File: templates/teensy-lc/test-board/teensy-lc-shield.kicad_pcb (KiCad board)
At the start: 2 copper layers, 1 part, among them J1 TEENSY LC

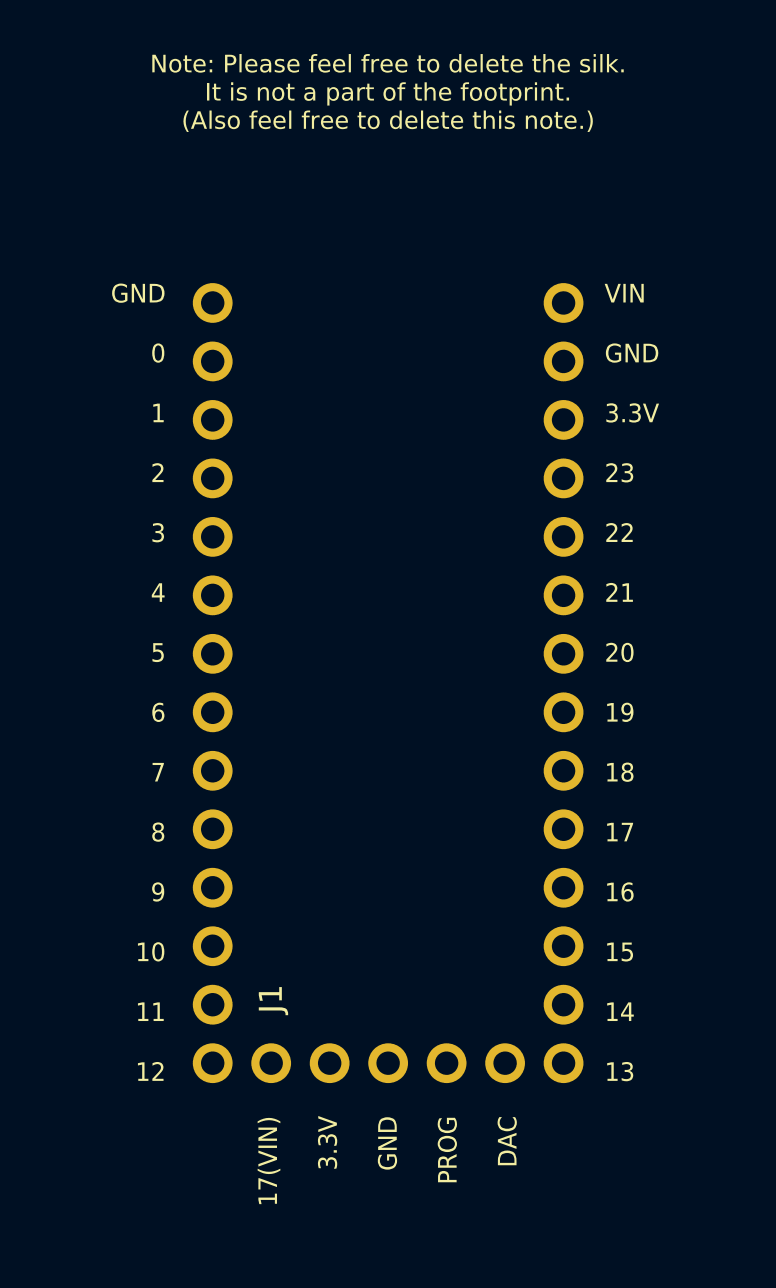
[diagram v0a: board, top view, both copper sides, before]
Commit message: Added Teensy LC bare template and test board.
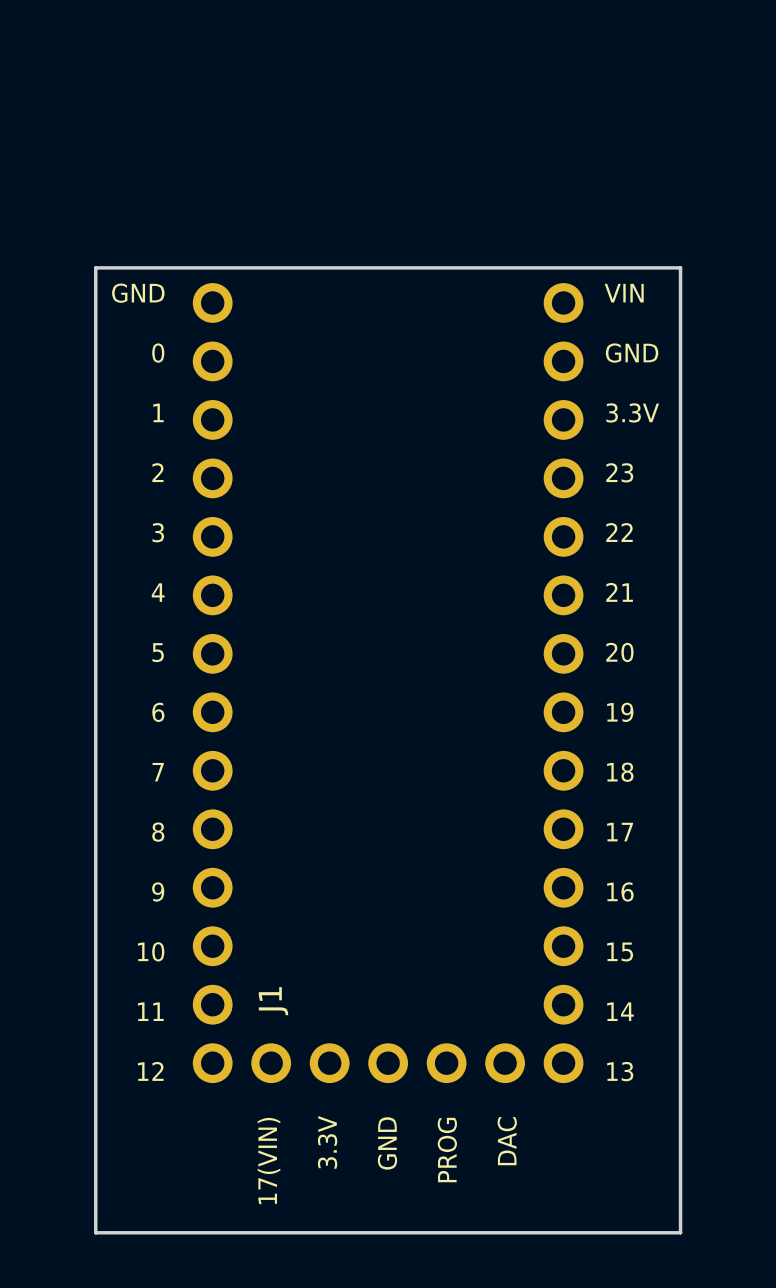
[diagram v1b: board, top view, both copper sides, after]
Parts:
- added REF**: Symbol_OSHW-Logo_SilkScreen, Wickerlib:Symbol_OSHW-Logo_SilkScreen, B.Cu at (102.9, 85.1)
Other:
- board outline added: 25.4 x 41.9 mm
- board text added: "TEMPLATE TEST BOARD"
- board text removed: "Note: Please feel free to delete the silk. It is not a part of the footprint. (Also feel free to delete this note.)"
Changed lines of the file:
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@@
 (kicad_pcb (version 4) (host pcbnew 4.0.1-3.201512221402+6198~38~ubuntu14.04.1-stable)
   (general
-    (links 3)
+    (links 0)
     (no_connects 3)
     (area 90.094999 71.043799 178.510001 123.265001)
     (thickness 1.6)
-    (drawings 21)
+    (drawings 25)
     (tracks 0)
     (zones 0)
-    (modules 1)
+    (modules 2)
     (nets 3)
   )
@@
     (pad 15 thru_hole circle (at 5.08 17.78) (size 1.7272 1.7272) (drill 1.016) (layers *.Cu *.Mask F.SilkS))
   )
-  (gr_text "Note: Please feel free to delete the silk.\nIt is not a part of the footprint.\n(Also feel free to delete this note.)" (at 102.87 63.5) (layer F.SilkS)
-    (effects (font (size 0.762 0.762) (thickness 0.1524)))
+  (module Wickerlib:Symbol_OSHW-Logo_SilkScreen (layer B.Cu)
+    (at 102.87 85.09 180)
+    (descr "Symbol, OSHW-Logo, Silk Screen,")
+    (tags "Symbol, OSHW-Logo, Silk Screen,")
+    (fp_text reference REF** (at 0.09906 4.38912 180) (layer B.SilkS) hide
+      (effects (font (size 1 1) (thickness 0.15)) (justify mirror))
+    )
+    (fp_text value Symbol_OSHW-Logo_SilkScreen (at 0.30988 -6.56082 180) (layer B.Fab)
+      (effects (font (size 1 1) (thickness 0.15)) (justify mirror))
+    )
+    (fp_line (start 1.66878 -2.68986) (end 2.02946 -4.16052) (layer B.SilkS) (width 0.15))
+    (fp_line (start 2.02946 -4.16052) (end 2.30886 -3.0988) (layer B.SilkS) (width 0.15))
+    (fp_line (start 2.30886 -3.0988) (end 2.61874 -4.17068) (layer B.SilkS) (width 0.15))
+    (fp_line (start 2.61874 -4.17068) (end 2.9591 -2.72034) (layer B.SilkS) (width 0.15))
+    (fp_line (start 0.24892 -3.38074) (end 1.03886 -3.37058) (layer B.SilkS) (width 0.15))
+    (fp_line (start 1.03886 -3.37058) (end 1.04902 -3.38074) (layer B.SilkS) (width 0.15))
+    (fp_line (start 1.04902 -3.38074) (end 1.04902 -3.37058) (layer B.SilkS) (width 0.15))
+    (fp_line (start 1.08966 -2.65938) (end 1.08966 -4.20116) (layer B.SilkS) (width 0.15))
+    (fp_line (start 0.20066 -2.64922) (end 0.20066 -4.21894) (layer B.SilkS) (width 0.15))
+    (fp_line (start 0.20066 -4.21894) (end 0.21082 -4.20878) (layer B.SilkS) (width 0.15))
+    (fp_line (start -0.35052 -2.75082) (end -0.70104 -2.66954) (layer B.SilkS) (width 0.15))
+    (fp_line (start -0.70104 -2.66954) (end -1.02108 -2.65938) (layer B.SilkS) (width 0.15))
+    (fp_line (start -1.02108 -2.65938) (end -1.25984 -2.86004) (layer B.SilkS) (width 0.15))
+    (fp_line (start -1.25984 -2.86004) (end -1.29032 -3.12928) (layer B.SilkS) (width 0.15))
+    (fp_line (start -1.29032 -3.12928) (end -1.04902 -3.37058) (layer B.SilkS) (width 0.15))
+    (fp_line (start -1.04902 -3.37058) (end -0.6604 -3.50012) (layer B.SilkS) (width 0.15))
+    (fp_line (start -0.6604 -3.50012) (end -0.48006 -3.66014) (layer B.SilkS) (width 0.15))
+    (fp_line (start -0.48006 -3.66014) (end -0.43942 -3.95986) (layer B.SilkS) (width 0.15))
+    (fp_line (start -0.43942 -3.95986) (end -0.67056 -4.18084) (layer B.SilkS) (width 0.15))
+    (fp_line (start -0.67056 -4.18084) (end -0.9906 -4.20878) (layer B.SilkS) (width 0.15))
+    (fp_line (start -0.9906 -4.20878) (end -1.34112 -4.09956) (layer B.SilkS) (width 0.15))
+    (fp_line (start -2.37998 -2.64922) (end -2.6289 -2.66954) (layer B.SilkS) (width 0.15))
+    (fp_line (start -2.6289 -2.66954) (end -2.8702 -2.91084) (layer B.SilkS) (width 0.15))
+    (fp_line (start -2.8702 -2.91084) (end -2.9591 -3.40106) (layer B.SilkS) (width 0.15))
+    (fp_line (start -2.9591 -3.40106) (end -2.93116 -3.74904) (layer B.SilkS) (width 0.15))
+    (fp_line (start -2.93116 -3.74904) (end -2.7305 -4.06908) (layer B.SilkS) (width 0.15))
+    (fp_line (start -2.7305 -4.06908) (end -2.47904 -4.191) (layer B.SilkS) (width 0.15))
+    (fp_line (start -2.47904 -4.191) (end -2.16916 -4.11988) (layer B.SilkS) (width 0.15))
+    (fp_line (start -2.16916 -4.11988) (end -1.95072 -3.93954) (layer B.SilkS) (width 0.15))
+    (fp_line (start -1.95072 -3.93954) (end -1.8796 -3.4798) (layer B.SilkS) (width 0.15))
+    (fp_line (start -1.8796 -3.4798) (end -1.9304 -3.07086) (layer B.SilkS) (width 0.15))
+    (fp_line (start -1.9304 -3.07086) (end -2.03962 -2.78892) (layer B.SilkS) (width 0.15))
+    (fp_line (start -2.03962 -2.78892) (end -2.4003 -2.65938) (layer B.SilkS) (width 0.15))
+    (fp_line (start -1.78054 -0.92964) (end -2.03962 -1.49098) (layer B.SilkS) (width 0.15))
+    (fp_line (start -2.03962 -1.49098) (end -1.50114 -2.00914) (layer B.SilkS) (width 0.15))
+    (fp_line (start -1.50114 -2.00914) (end -0.98044 -1.7399) (layer B.SilkS) (width 0.15))
+    (fp_line (start -0.98044 -1.7399) (end -0.70104 -1.89992) (layer B.SilkS) (width 0.15))
+    (fp_line (start 0.73914 -1.8796) (end 1.06934 -1.6891) (layer B.SilkS) (width 0.15))
+    (fp_line (start 1.06934 -1.6891) (end 1.50876 -2.0193) (layer B.SilkS) (width 0.15))
+    (fp_line (start 1.50876 -2.0193) (end 1.9812 -1.52908) (layer B.SilkS) (width 0.15))
+    (fp_line (start 1.9812 -1.52908) (end 1.69926 -1.04902) (layer B.SilkS) (width 0.15))
+    (fp_line (start 1.69926 -1.04902) (end 1.88976 -0.57912) (layer B.SilkS) (width 0.15))
+    (fp_line (start 1.88976 -0.57912) (end 2.49936 -0.39116) (layer B.SilkS) (width 0.15))
+    (fp_line (start 2.49936 -0.39116) (end 2.49936 0.28956) (layer B.SilkS) (width 0.15))
+    (fp_line (start 2.49936 0.28956) (end 1.94056 0.42926) (layer B.SilkS) (width 0.15))
+    (fp_line (start 1.94056 0.42926) (end 1.7399 1.00076) (layer B.SilkS) (width 0.15))
+    (fp_line (start 1.7399 1.00076) (end 2.00914 1.47066) (layer B.SilkS) (width 0.15))
+    (fp_line (start 2.00914 1.47066) (end 1.53924 1.9812) (layer B.SilkS) (width 0.15))
+    (fp_line (start 1.53924 1.9812) (end 1.02108 1.71958) (layer B.SilkS) (width 0.15))
+    (fp_line (start 1.02108 1.71958) (end 0.55118 1.92024) (layer B.SilkS) (width 0.15))
+    (fp_line (start 0.55118 1.92024) (end 0.381 2.46126) (layer B.SilkS) (width 0.15))
+    (fp_line (start 0.381 2.46126) (end -0.30988 2.47904) (layer B.SilkS) (width 0.15))
+    (fp_line (start -0.30988 2.47904) (end -0.5207 1.9304) (layer B.SilkS) (width 0.15))
+    (fp_line (start -0.5207 1.9304) (end -0.9398 1.76022) (layer B.SilkS) (width 0.15))
+    (fp_line (start -0.9398 1.76022) (end -1.49098 2.02946) (layer B.SilkS) (width 0.15))
+    (fp_line (start -1.49098 2.02946) (end -2.00914 1.50114) (layer B.SilkS) (width 0.15))
+    (fp_line (start -2.00914 1.50114) (end -1.76022 0.96012) (layer B.SilkS) (width 0.15))
+    (fp_line (start -1.76022 0.96012) (end -1.9304 0.48006) (layer B.SilkS) (width 0.15))
+    (fp_line (start -1.9304 0.48006) (end -2.47904 0.381) (layer B.SilkS) (width 0.15))
+    (fp_line (start -2.47904 0.381) (end -2.4892 -0.32004) (layer B.SilkS) (width 0.15))
+    (fp_line (start -2.4892 -0.32004) (end -1.9304 -0.5207) (layer B.SilkS) (width 0.15))
+    (fp_line (start -1.9304 -0.5207) (end -1.7907 -0.91948) (layer B.SilkS) (width 0.15))
+    (fp_line (start 0.35052 -0.89916) (end 0.65024 -0.7493) (layer B.SilkS) (width 0.15))
+    (fp_line (start 0.65024 -0.7493) (end 0.8509 -0.55118) (layer B.SilkS) (width 0.15))
+    (fp_line (start 0.8509 -0.55118) (end 1.00076 -0.14986) (layer B.SilkS) (width 0.15))
+    (fp_line (start 1.00076 -0.14986) (end 1.00076 0.24892) (layer B.SilkS) (width 0.15))
+    (fp_line (start 1.00076 0.24892) (end 0.8509 0.59944) (layer B.SilkS) (width 0.15))
+    (fp_line (start 0.8509 0.59944) (end 0.39878 0.94996) (layer B.SilkS) (width 0.15))
+    (fp_line (start 0.39878 0.94996) (end -0.0508 1.00076) (layer B.SilkS) (width 0.15))
+    (fp_line (start -0.0508 1.00076) (end -0.44958 0.89916) (layer B.SilkS) (width 0.15))
+    (fp_line (start -0.44958 0.89916) (end -0.8509 0.55118) (layer B.SilkS) (width 0.15))
+    (fp_line (start -0.8509 0.55118) (end -1.00076 0.09906) (layer B.SilkS) (width 0.15))
+    (fp_line (start -1.00076 0.09906) (end -0.94996 -0.39878) (layer B.SilkS) (width 0.15))
+    (fp_line (start -0.94996 -0.39878) (end -0.70104 -0.70104) (layer B.SilkS) (width 0.15))
+    (fp_line (start -0.70104 -0.70104) (end -0.35052 -0.89916) (layer B.SilkS) (width 0.15))
+    (fp_line (start -0.35052 -0.89916) (end -0.70104 -1.89992) (layer B.SilkS) (width 0.15))
+    (fp_line (start 0.35052 -0.89916) (end 0.7493 -1.89992) (layer B.SilkS) (width 0.15))
+  )
+  (gr_line (start 90.17 113.03) (end 90.17 71.12) (layer Edge.Cuts) (width 0.15))
+  (gr_line (start 115.57 113.03) (end 90.17 113.03) (layer Edge.Cuts) (width 0.15))
+  (gr_line (start 115.57 71.12) (end 115.57 113.03) (layer Edge.Cuts) (width 0.15))
+  (gr_line (start 90.17 71.12) (end 115.57 71.12) (layer Edge.Cuts) (width 0.15))
+  (gr_text "TEMPLATE\nTEST BOARD" (at 102.87 101.6) (layer B.SilkS)
+    (effects (font (size 1 1) (thickness 0.15)) (justify mirror))
+  )
+  (gr_text "17(VIN)\n\n3.3V\n\nGND\n\nPROG\n\nDAC" (at 102.87 107.95 90) (layer F.SilkS)
+    (effects (font (size 0.80772 0.762) (thickness 0.1524)) (justify right))
+  )
+  (gr_text "GND\n\n0\n\n1\n\n2\n\n3\n\n4\n\n5\n\n6\n\n7\n\n8\n\n9\n\n10\n\n11\n\n12" (at 93.218 89.154) (layer F.SilkS)
+    (effects (font (size 0.80772 0.762) (thickness 0.1524)) (justify right))
   )
   (gr_text "VIN\n\nGND\n\n3.3V\n\n23\n\n22\n\n21\n\n20\n\n19\n\n18\n\n17\n\n16\n\n15\n\n14\n\n13\n" (at 112.268 89.154) (layer F.SilkS)
     (effects (font (size 0.80772 0.762) (thickness 0.1524)) (justify left))
   )
-  (gr_text "GND\n\n0\n\n1\n\n2\n\n3\n\n4\n\n5\n\n6\n\n7\n\n8\n\n9\n\n10\n\n11\n\n12" (at 93.218 89.154) (layer F.SilkS)
-    (effects (font (size 0.80772 0.762) (thickness 0.1524)) (justify right))
-  )
-  (gr_text "17(VIN)\n\n3.3V\n\nGND\n\nPROG\n\nDAC" (at 102.87 107.95 90) (layer F.SilkS)
-    (effects (font (size 0.80772 0.762) (thickness 0.1524)) (justify right))
-  )
   (gr_circle (center 117.348 76.962) (end 118.618 76.962) (layer Dwgs.User) (width 0.15))
